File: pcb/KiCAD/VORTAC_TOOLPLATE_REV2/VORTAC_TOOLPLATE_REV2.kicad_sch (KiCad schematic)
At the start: 6 parts, among them J1 Conn_01x05, J2 Conn_01x02, J3 Conn_01x03

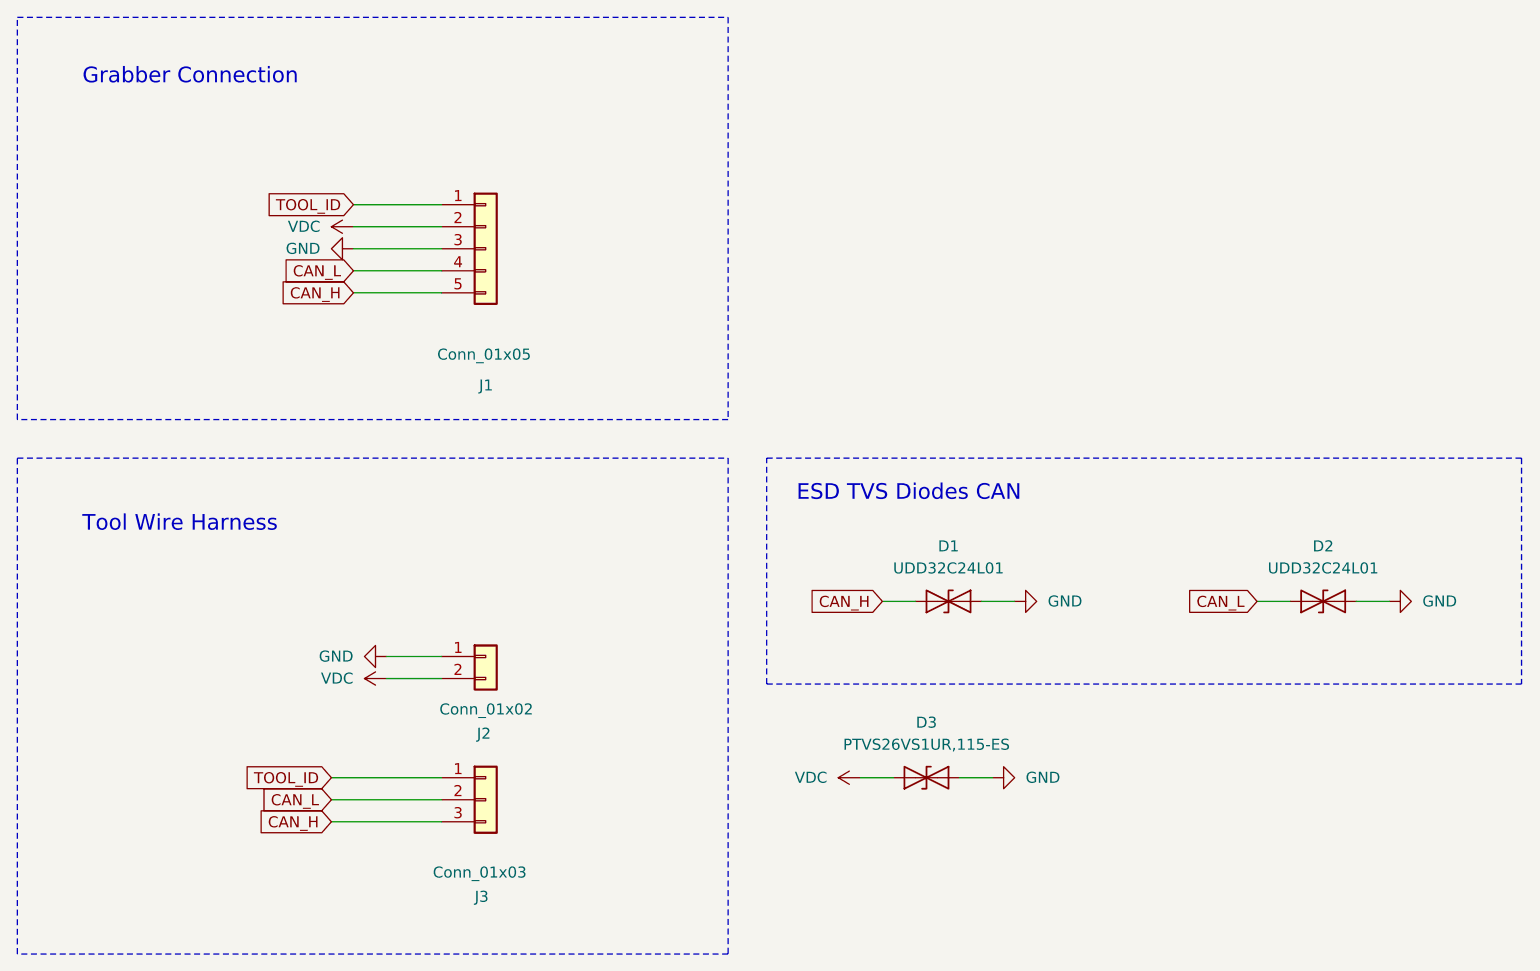
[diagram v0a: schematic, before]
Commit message: Added VORTAC_TOOLPLATE_REV2
Modified VORTAC_TOOL
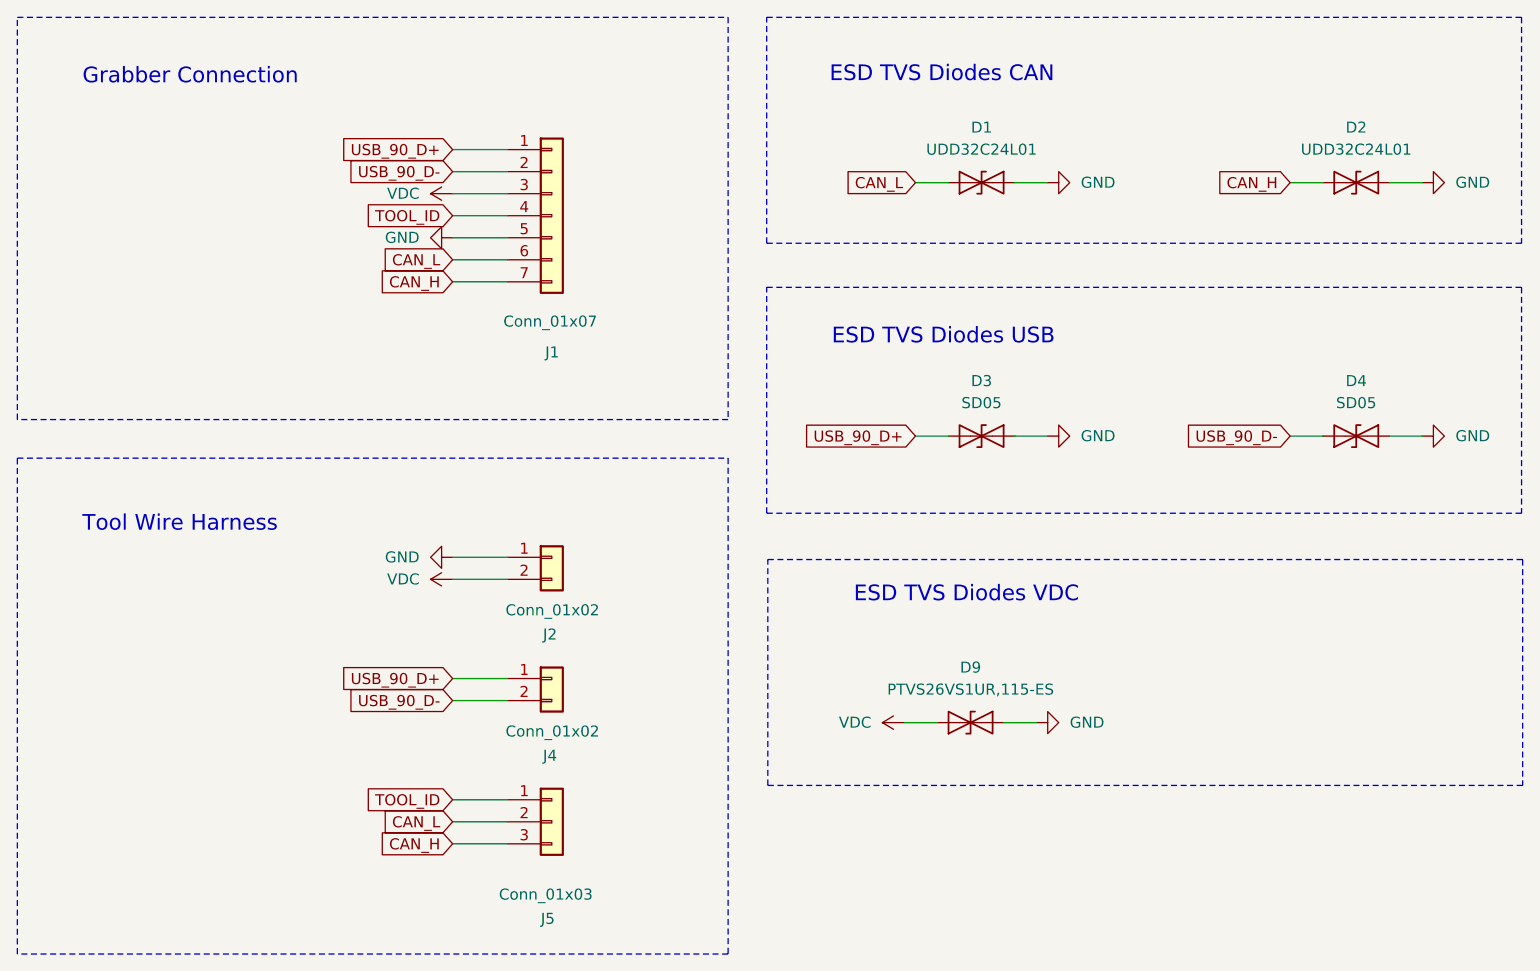
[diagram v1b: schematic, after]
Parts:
- removed J3: Conn_01x03, Vortac:Toolplate_Solderpoint_01x03_Data_Small, symbol Connector_Generic:Conn_01x03
- added D3, D4: SD05, Diode_SMD:D_SOD-323, symbol Diode:SD24_SOD323
- added J4: Conn_01x02, Vortac:Toolplate_Solderpoint_01x02_Data_Small, symbol Connector_Generic:Conn_01x02
- added J5: Conn_01x03, Vortac:Toolplate_Solderpoint_01x03_Data_Small, symbol Connector_Generic:Conn_01x03
- J1: value Conn_01x05 -> Conn_01x07; footprint Vortac:mill-max-0881-1-15-20-82-14-11-0_LandingPads_ContactPad_1x5 -> Vortac:mill-max-0881-1-15-20-82-14-11-0_LandingPads_ContactPad_PTH_2x1.5x1; symbol Connector_Generic:Conn_01x05 -> Connector_Generic:Conn_01x07; now in the parts list
- J2: now in the parts list
- renumbered D3 to D9
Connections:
- net CAN_H: now also D2.2 (A2), J1.7 (Pin_7), J5.3 (Pin_3); no longer D1.2 (A2), J1.5 (Pin_5)
- net CAN_L: now also D1.2 (A2), J1.6 (Pin_6), J5.2 (Pin_2); no longer D2.2 (A2), J1.4 (Pin_4)
- net GND: now also J1.5 (Pin_5), D3.1 (A1), D4.1 (A1); no longer J1.3 (Pin_3)
- net TOOL_ID: now also J1.4 (Pin_4), J5.1 (Pin_1); no longer J1.1 (Pin_1)
- net VDC: now also J1.3 (Pin_3); no longer J1.2 (Pin_2)
- new net USB_90_D+: D3.2 (A2), J1.1 (Pin_1), J4.1 (Pin_1)
- new net USB_90_D-: D4.2 (A2), J1.2 (Pin_2), J4.2 (Pin_2)
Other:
- note added: "ESD TVS Diodes USB"
- note added: "ESD TVS Diodes VDC"
- moved on the sheet: D1, D2, D9, J2

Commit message: (Hopefully) Finalized DOCK, TOOL and TOOLPLATE REV2 for ordering
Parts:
- renumbered D9 to D5, J4 to J3, J5 to J4
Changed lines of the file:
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@@
 		(dnp no)
 		(fields_autoplaced yes)
-		(property "Reference" "#PWR06"
+		(property "Reference" "#PWR08"
 			(at 73.66 83.82 0)
 			(effects
@@
 			(project "VORTAC_TOOLPLATE_REV1"
 				(path "/b23b3086-82ed-4285-9d49-d03b4e41a1a0"
-					(reference "#PWR06")
+					(reference "#PWR08")
 					(unit 1)
 				)
@@
 		(on_board yes)
 		(dnp no)
-		(property "Reference" "J5"
+		(property "Reference" "J4"
 			(at 80.01 122.936 0)
 			(effects
@@
 			(project "VORTAC_TOOLPLATE_REV2"
 				(path "/b23b3086-82ed-4285-9d49-d03b4e41a1a0"
-					(reference "J5")
+					(reference "J4")
 					(unit 1)
 				)
@@
 		(dnp no)
 		(fields_autoplaced yes)
-		(property "Reference" "#PWR09"
+		(property "Reference" "#PWR01"
 			(at 144.78 38.1 0)
 			(effects
@@
 			(project "VORTAC_TOOLPLATE_REV1"
 				(path "/b23b3086-82ed-4285-9d49-d03b4e41a1a0"
-					(reference "#PWR09")
+					(reference "#PWR01")
 					(unit 1)
 				)
@@
 		(dnp no)
 		(fields_autoplaced yes)
-		(property "Reference" "#PWR010"
+		(property "Reference" "#PWR02"
 			(at 187.96 38.1 0)
 			(effects
@@
 			(project "VORTAC_TOOLPLATE_REV1"
 				(path "/b23b3086-82ed-4285-9d49-d03b4e41a1a0"
-					(reference "#PWR010")
+					(reference "#PWR02")
 					(unit 1)
 				)
@@
 		(dnp no)
 		(fields_autoplaced yes)
-		(property "Reference" "D9"
+		(property "Reference" "D5"
 			(at 129.54 93.98 0)
 			(effects
@@
 			(project "VORTAC_TOOLPLATE_REV1"
 				(path "/b23b3086-82ed-4285-9d49-d03b4e41a1a0"
-					(reference "D9")
+					(reference "D5")
 					(unit 1)
 				)
@@
 		(dnp no)
 		(fields_autoplaced yes)
-		(property "Reference" "#PWR08"
+		(property "Reference" "#PWR06"
 			(at 187.96 67.31 0)
 			(effects
@@
 			(project "VORTAC_TOOLPLATE_REV1"
 				(path "/b23b3086-82ed-4285-9d49-d03b4e41a1a0"
-					(reference "#PWR08")
+					(reference "#PWR06")
 					(unit 1)
 				)
@@
 		(on_board yes)
 		(dnp no)
-		(property "Reference" "J4"
+		(property "Reference" "J3"
 			(at 80.264 104.14 0)
 			(effects
@@
 			(project "VORTAC_TOOLPLATE_REV2"
 				(path "/b23b3086-82ed-4285-9d49-d03b4e41a1a0"
-					(reference "J4")
+					(reference "J3")
 					(unit 1)
 				)
@@
 		(dnp no)
 		(fields_autoplaced yes)
-		(property "Reference" "#PWR01"
+		(property "Reference" "#PWR04"
 			(at 63.5 44.45 0)
 			(effects
@@
 			(project ""
 				(path "/b23b3086-82ed-4285-9d49-d03b4e41a1a0"
-					(reference "#PWR01")
+					(reference "#PWR04")
 					(unit 1)
 				)
@@
 		(dnp no)
 		(fields_autoplaced yes)
-		(property "Reference" "#PWR012"
+		(property "Reference" "#PWR010"
 			(at 143.51 100.33 0)
 			(effects
@@
 			(project "VORTAC_TOOLPLATE_REV1"
 				(path "/b23b3086-82ed-4285-9d49-d03b4e41a1a0"
-					(reference "#PWR012")
+					(reference "#PWR010")
 					(unit 1)
 				)
@@
 		(dnp no)
 		(fields_autoplaced yes)
-		(property "Reference" "#PWR011"
+		(property "Reference" "#PWR09"
 			(at 125.73 100.33 0)
 			(effects
@@
 			(project "VORTAC_TOOLPLATE_REV1"
 				(path "/b23b3086-82ed-4285-9d49-d03b4e41a1a0"
-					(reference "#PWR011")
+					(reference "#PWR09")
 					(unit 1)
 				)
@@
 		(dnp no)
 		(fields_autoplaced yes)
-		(property "Reference" "#PWR02"
+		(property "Reference" "#PWR03"
 			(at 73.66 39.37 0)
 			(effects
@@
 			(project ""
 				(path "/b23b3086-82ed-4285-9d49-d03b4e41a1a0"
-					(reference "#PWR02")
+					(reference "#PWR03")
 					(unit 1)
 				)
@@
 		(dnp no)
 		(fields_autoplaced yes)
-		(property "Reference" "#PWR05"
+		(property "Reference" "#PWR07"
 			(at 63.5 81.28 0)
 			(effects
@@
 			(project "VORTAC_TOOLPLATE_REV1"
 				(path "/b23b3086-82ed-4285-9d49-d03b4e41a1a0"
-					(reference "#PWR05")
+					(reference "#PWR07")
 					(unit 1)
 				)
@@
 		(dnp no)
 		(fields_autoplaced yes)
-		(property "Reference" "#PWR07"
+		(property "Reference" "#PWR05"
 			(at 144.78 67.31 0)
 			(effects
@@
 			(project "VORTAC_TOOLPLATE_REV1"
 				(path "/b23b3086-82ed-4285-9d49-d03b4e41a1a0"
-					(reference "#PWR07")
-					(unit 1)
-				)
+					(reference "#PWR05")
+					(unit 1)
+				)
